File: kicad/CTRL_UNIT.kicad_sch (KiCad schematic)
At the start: 6 parts, among them U3 SN74LVC2G157DCU3, U4 SN74LVC2G157DCU3

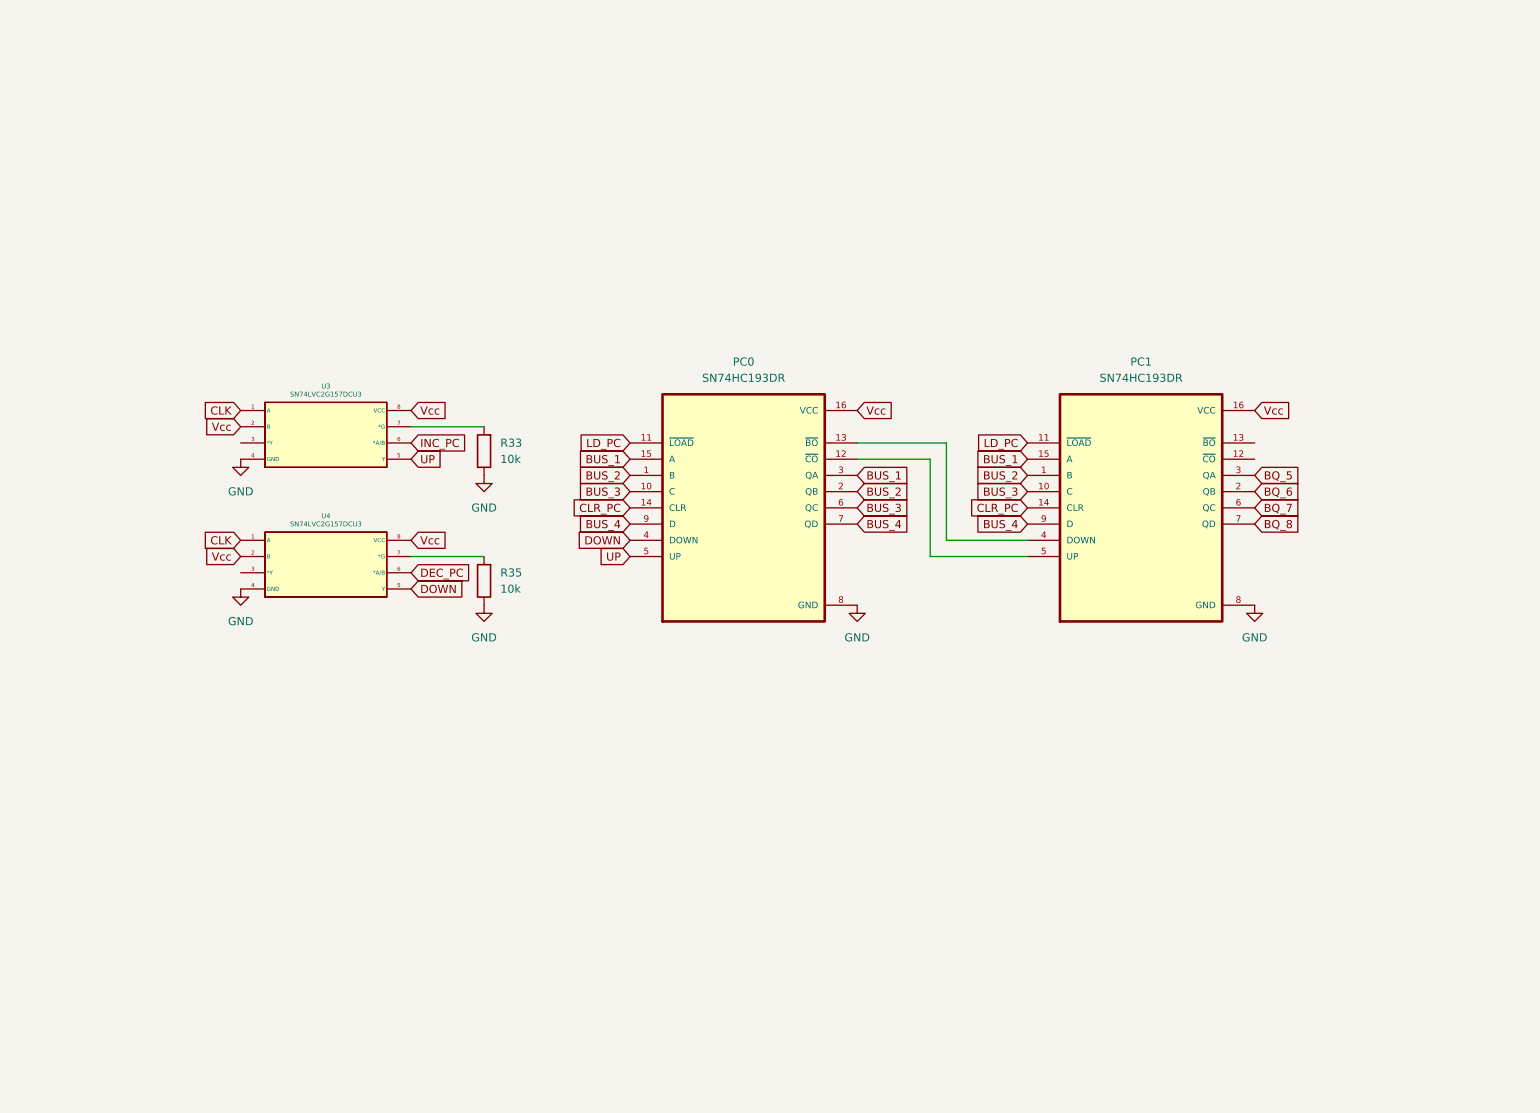
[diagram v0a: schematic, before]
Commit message: update schematic
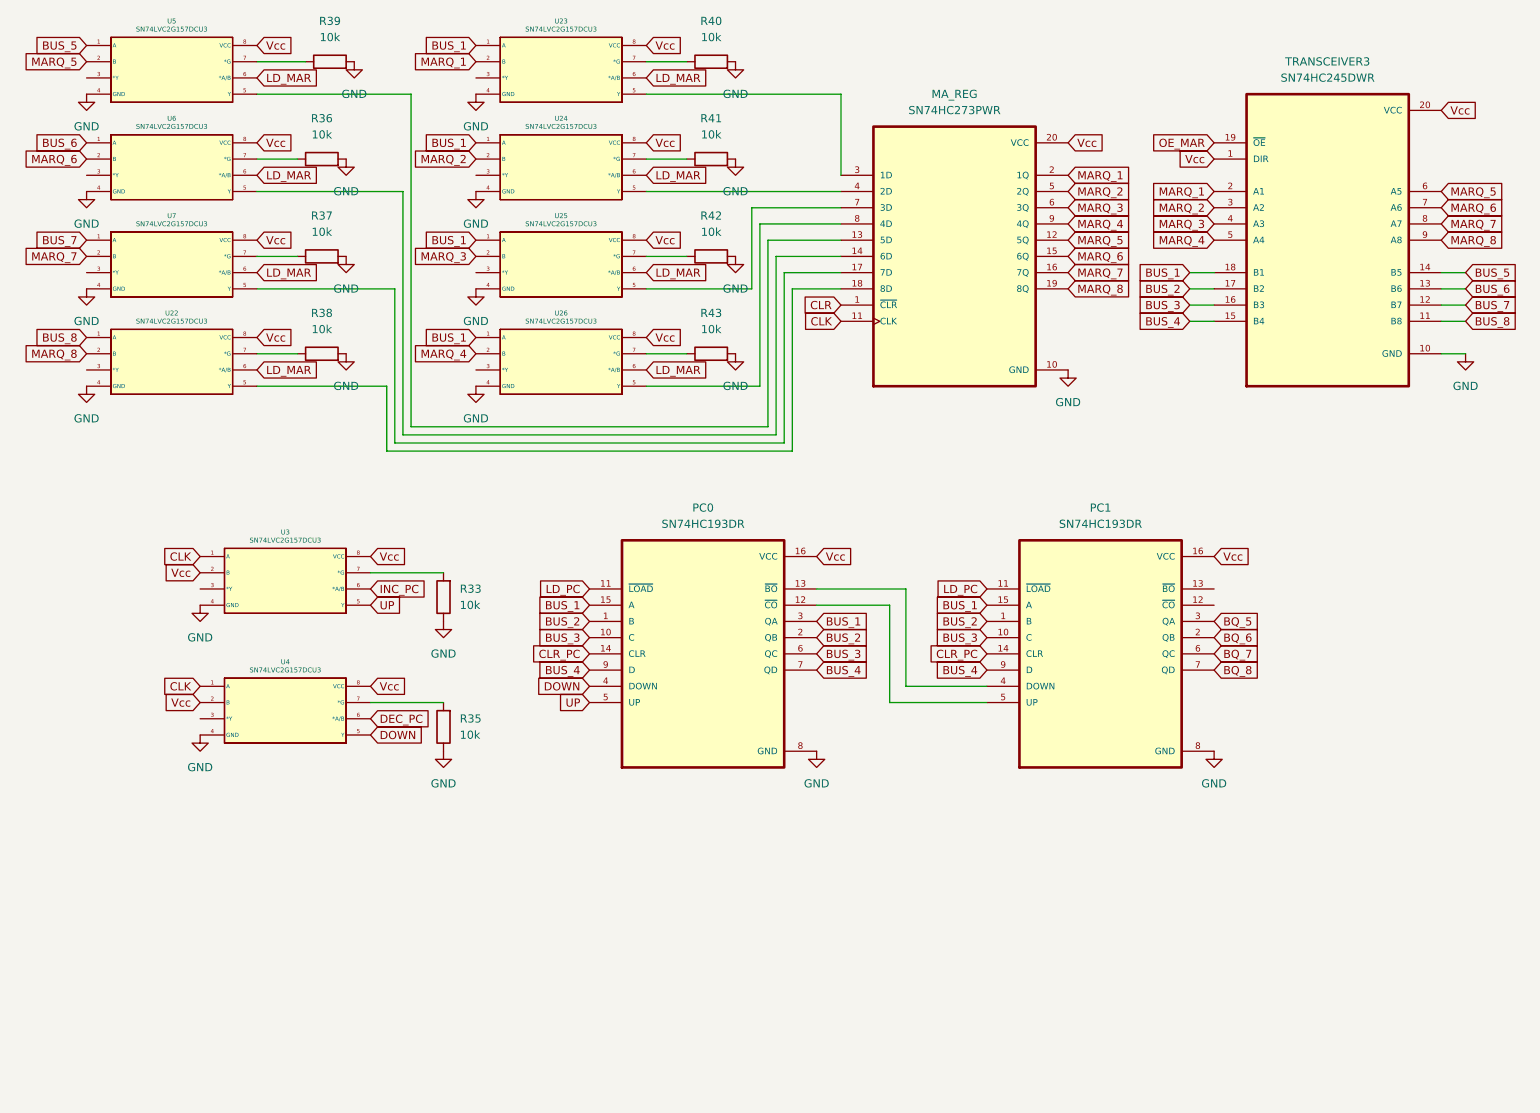
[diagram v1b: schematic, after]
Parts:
- added MA_REG: SN74HC273PWR, SN74HC273PWR:SOP65P640X120-20N, symbol SN74HC273PWR:SN74HC273PWR
- added R36, R37, R38, R39, R40, R41, R42, R43: 10k, symbol Device:R
- added TRANSCEIVER3: SN74HC245DWR, SN74HC245DWR:SOIC127P1030X265-20N, symbol SN74HC245DWR:SN74HC245DWR
- added U22, U23, U24, U25, U26, U5, U6, U7: SN74LVC2G157DCU3, DCU8, symbol SN74LVC2G157DCU3:SN74LVC2G157DCU3
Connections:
- net BUS_1: now also TRANSCEIVER3.18 (B1), U23.1 (A), U24.1 (A), U25.1 (A), U26.1 (A)
- net BUS_2: now also TRANSCEIVER3.17 (B2)
- net BUS_3: now also TRANSCEIVER3.16 (B3)
- net BUS_4: now also TRANSCEIVER3.15 (B4)
- net CLK: now also MA_REG.11 (CLK)
- net GND: now also MA_REG.10 (GND), R36.2, R37.2, R38.2, R39.2, R40.2, R41.2, R42.2, R43.2, TRANSCEIVER3.10 (GND), U22.4 (GND), U23.4 (GND), U24.4 (GND), U25.4 (GND), U26.4 (GND), U5.4 (GND), U6.4 (GND), U7.4 (GND)
- net Vcc: now also MA_REG.20 (VCC), TRANSCEIVER3.1 (DIR), TRANSCEIVER3.20 (VCC), U22.8 (VCC), U23.8 (VCC), U24.8 (VCC), U25.8 (VCC), U26.8 (VCC), U5.8 (VCC), U6.8 (VCC), U7.8 (VCC)
- new net: MA_REG.13 (5D), U5.5 (Y)
- new net: R39.1, U5.7 (*G)
- new net: MA_REG.17 (7D), U7.5 (Y)
- new net: R37.1, U7.7 (*G)
- new net: MA_REG.3 (1D), U23.5 (Y)
- new net: R40.1, U23.7 (*G)
- new net: MA_REG.4 (2D), U24.5 (Y)
- new net: R41.1, U24.7 (*G)
- new net: MA_REG.18 (8D), U22.5 (Y)
- new net: R38.1, U22.7 (*G)
- new net: MA_REG.7 (3D), U25.5 (Y)
- new net: R42.1, U25.7 (*G)
- new net: R36.1, U6.7 (*G)
- new net: MA_REG.8 (4D), U26.5 (Y)
- new net: R43.1, U26.7 (*G)
- new net: MA_REG.14 (6D), U6.5 (Y)
- new net BUS_5: TRANSCEIVER3.14 (B5), U5.1 (A)
- new net BUS_6: TRANSCEIVER3.13 (B6), U6.1 (A)
- new net BUS_7: TRANSCEIVER3.12 (B7), U7.1 (A)
- new net BUS_8: TRANSCEIVER3.11 (B8), U22.1 (A)
- new net CLR: MA_REG.1 (~{CLR})
- new net LD_MAR: U22.6 (*A/B), U23.6 (*A/B), U24.6 (*A/B), U25.6 (*A/B), U26.6 (*A/B), U5.6 (*A/B), U6.6 (*A/B), U7.6 (*A/B)
- new net MARQ_1: MA_REG.2 (1Q), TRANSCEIVER3.2 (A1), U23.2 (B)
- new net MARQ_2: MA_REG.5 (2Q), TRANSCEIVER3.3 (A2), U24.2 (B)
- new net MARQ_3: MA_REG.6 (3Q), TRANSCEIVER3.4 (A3), U25.2 (B)
- new net MARQ_4: MA_REG.9 (4Q), TRANSCEIVER3.5 (A4), U26.2 (B)
- new net MARQ_5: MA_REG.12 (5Q), TRANSCEIVER3.6 (A5), U5.2 (B)
- new net MARQ_6: MA_REG.15 (6Q), TRANSCEIVER3.7 (A6), U6.2 (B)
- new net MARQ_7: MA_REG.16 (7Q), TRANSCEIVER3.8 (A7), U7.2 (B)
- new net MARQ_8: MA_REG.19 (8Q), TRANSCEIVER3.9 (A8), U22.2 (B)
- new net OE_MAR: TRANSCEIVER3.19 (~{OE})
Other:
- moved on the sheet: PC0, PC1, R33, R35, U3, U4

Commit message: add instruction decoder
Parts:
- added U36: CD4029BM96, D16, symbol CD4029BM96:CD4029BM96
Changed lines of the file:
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@@
+		)
+	)
+	(symbol
+		(lib_id "CD4029BM96:CD4029BM96")
+		(at 48.26 134.62 0)
+		(unit 1)
+		(exclude_from_sim no)
+		(in_bom yes)
+		(on_board yes)
+		(dnp no)
+		(fields_autoplaced yes)
+		(property "Reference" "U36"
+			(at 95.25 156.21 0)
+			(effects
+				(font
+					(size 1.524 1.524)
+				)
+			)
+		)
+		(property "Value" "CD4029BM96"
+			(at 95.25 158.75 0)
+			(effects
+				(font
+					(size 1.524 1.524)
+				)
+			)
+		)
+		(property "Footprint" "D16"
+			(at 46.99 166.37 0)
+			(effects
+				(font
+					(size 1.27 1.27)
+					(italic yes)
+				)
+				(hide yes)
+			)
+		)
+		(property "Datasheet" "https://www.ti.com/lit/gpn/cd4029b"
+			(at 48.26 134.62 0)
+			(effects
+				(font
+					(size 1.27 1.27)
+					(italic yes)
+				)
+				(hide yes)
+			)
+		)
+		(property "Description" ""
+			(at 48.26 134.62 0)
+			(effects
+				(font
+					(size 1.27 1.27)
+				)
+				(hide yes)
+			)
+		)
+		(pin "14"
+		)
+		(pin "12"
+		)
+		(pin "16"
+		)
+		(pin "1"
+		)
+		(pin "13"
+		)
+		(pin "4"
+		)
+		(pin "5"
+		)
+		(pin "9"
+		)
+		(pin "7"
+		)
+		(pin "11"
+		)
+		(pin "3"
+		)
+		(pin "10"
+		)
+		(pin "6"
+		)
+		(pin "8"
+		)
+		(pin "2"
+		)
+		(pin "15"
+		)
+		(instances
+			(project ""
+				(path "/d90612be-a4bb-4b59-8bc6-93e31ea1f515/117e83a4-c196-48c8-a5be-455f653a576a"
+					(reference "U36")
+					(unit 1)
+				)
+			)
 		)
 	)
